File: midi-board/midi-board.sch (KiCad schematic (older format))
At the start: 39 parts, among them J1 MIDI OUT, J2 MIDI IN, J3 Qwiic, J4 A0, J5 A1, J6 Qwiic, J7 UART, U1 74LVC1G06, U2 MCP1X0-315, U3 TLP185(SE, U4 SC16IS740, X1 SG-5032CAN

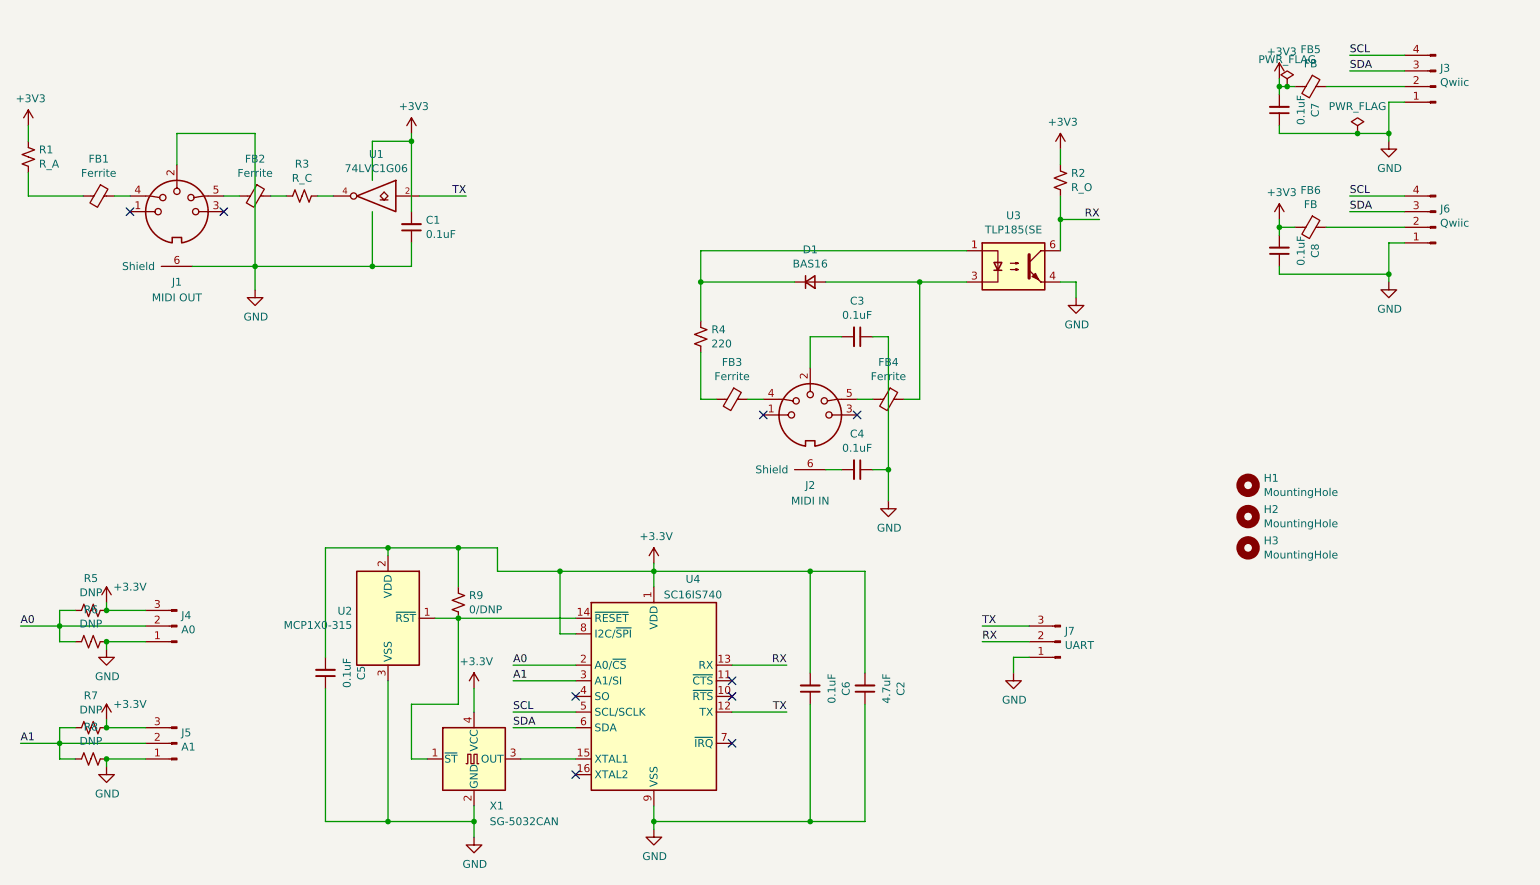
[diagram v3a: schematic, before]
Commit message: MIDI board Rev 1 changes
* Standardize mounting hole spacing
* Change 74LVC1G06 to 74LVC1G07 in schematic
* Expose ~IRQ headers
* Increase Qwiic header space
* Improve TLP185(SE footprint; remove unused pads, label orientation
* Bring I2C out on a header.
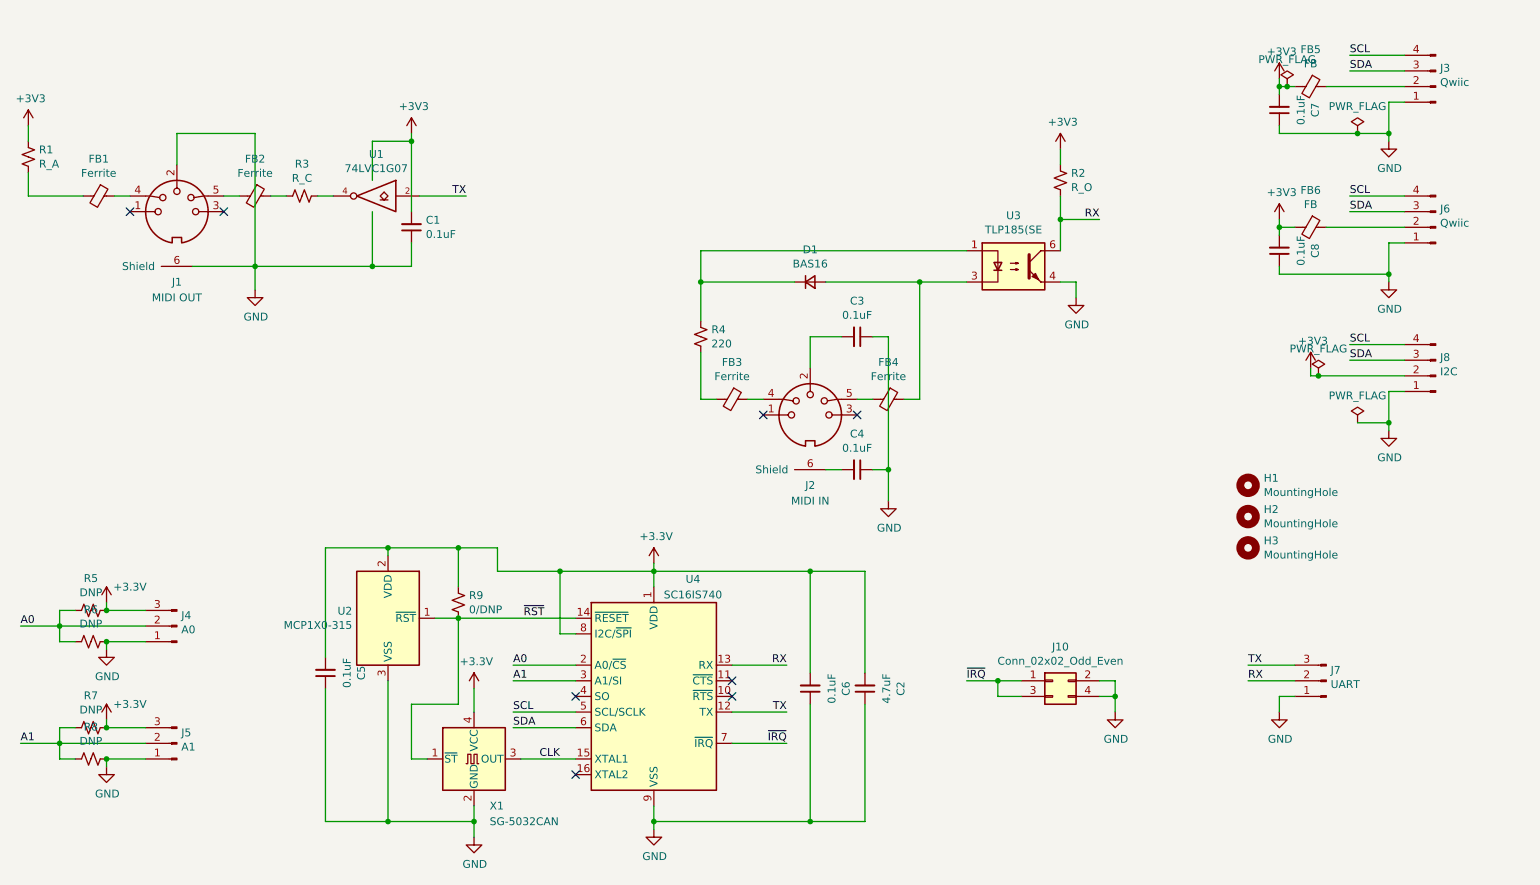
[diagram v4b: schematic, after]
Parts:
- added J10: Conn_02x02_Odd_Even, Pin_Headers:Pin_Header_Straight_2x02_Pitch2.54mm, symbol Connector_Generic:Conn_02x02_Odd_Even
- added J8: I2C, Pin_Headers:Pin_Header_Straight_1x04_Pitch2.54mm, symbol Connector:Conn_01x04_Male
- H1, H2, H3: footprint Mounting_Holes:MountingHole_3.2mm_M3 -> Mounting_Holes:MountingHole_3.2mm_M3_Pad_Via
- U1: value 74LVC1G06 -> 74LVC1G07
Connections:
- net +3V3: now also J8.2 (Pin_2)
- net GND: now also J10.2 (Pin_2), J10.4 (Pin_4), J8.1 (Pin_1)
- net SCL: now also J8.4 (Pin_4)
- net SDA: now also J8.3 (Pin_3)
- net ~RST: now reaches R9.1, U2.1 (~RST), U4.14 (~RESET), X1.1 (~ST)
- net CLK: now reaches U4.15 (XTAL1), X1.3 (OUT)
- net ~IRQ: now reaches U4.7 (~IRQ)
- net ~IRQ: now also J10.1 (Pin_1), J10.3 (Pin_3)
- no-connect marks 9 -> 8
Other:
- moved on the sheet: J7
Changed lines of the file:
@@
 P 3400 1950
 F 0 "U1" H 3375 2217 50  0000 C CNN
-F 1 "74LVC1G06" H 3375 2126 50  0000 C CNN
+F 1 "74LVC1G07" H 3375 2126 50  0000 C CNN
 F 2 "TO_SOT_Packages_SMD:SOT-353_SC-70-5_Handsoldering" H 3400 1950 50  0001 C CNN
 F 3 "http://www.ti.com/lit/sg/scyt129e/scyt129e.pdf" H 3400 1950 50  0001 C CNN
@@
 F 0 "H1" H 9100 3846 50  0000 L CNN
 F 1 "MountingHole" H 9100 3755 50  0000 L CNN
-F 2 "Mounting_Holes:MountingHole_3.2mm_M3" H 9000 3800 50  0001 C CNN
+F 2 "Mounting_Holes:MountingHole_3.2mm_M3_Pad_Via" H 9000 3800 50  0001 C CNN
 F 3 "~" H 9000 3800 50  0001 C CNN
 	1    9000 3800
@@
 F 0 "H2" H 9100 4046 50  0000 L CNN
 F 1 "MountingHole" H 9100 3955 50  0000 L CNN
-F 2 "Mounting_Holes:MountingHole_3.2mm_M3" H 9000 4000 50  0001 C CNN
+F 2 "Mounting_Holes:MountingHole_3.2mm_M3_Pad_Via" H 9000 4000 50  0001 C CNN
 F 3 "~" H 9000 4000 50  0001 C CNN
 	1    9000 4000
@@
 F 0 "H3" H 9100 4246 50  0000 L CNN
 F 1 "MountingHole" H 9100 4155 50  0000 L CNN
-F 2 "Mounting_Holes:MountingHole_3.2mm_M3" H 9000 4200 50  0001 C CNN
+F 2 "Mounting_Holes:MountingHole_3.2mm_M3_Pad_Via" H 9000 4200 50  0001 C CNN
 F 3 "~" H 9000 4200 50  0001 C CNN
 	1    9000 4200
@@
 NoConn ~ 5700 5150
 NoConn ~ 5700 5050
-NoConn ~ 5700 5450
 NoConn ~ 4700 5650
 Wire Wire Line
@@
 L Connector:Conn_01x03_Male J7
 U 1 1 5FFC58E3
-P 7800 4800
-F 0 "J7" H 7772 4732 50  0000 R CNN
-F 1 "UART" H 7772 4823 50  0000 R CNN
-F 2 "Pin_Headers:Pin_Header_Straight_1x03_Pitch2.54mm" H 7800 4800 50  0001 C CNN
-F 3 "~" H 7800 4800 50  0001 C CNN
-	1    7800 4800
-	-1   0    0    1
-$EndComp
-Wire Wire Line
-	7600 4900 7500 4900
-Wire Wire Line
-	7500 4900 7500 5000
+P 9500 5050
+F 0 "J7" H 9472 4982 50  0000 R CNN
+F 1 "UART" H 9472 5073 50  0000 R CNN
+F 2 "Pin_Headers:Pin_Header_Straight_1x03_Pitch2.54mm" H 9500 5050 50  0001 C CNN
+F 3 "~" H 9500 5050 50  0001 C CNN
+	1    9500 5050
+	-1   0    0    1
+$EndComp
+Wire Wire Line
+	9300 5150 9200 5150
+Wire Wire Line
+	9200 5150 9200 5250
 $Comp
 L power:GND #PWR0119
 U 1 1 5FFCB599
-P 7500 5000
-F 0 "#PWR0119" H 7500 4750 50  0001 C CNN
-F 1 "GND" H 7505 4827 50  0000 C CNN
-F 2 "" H 7500 5000 50  0001 C CNN
-F 3 "" H 7500 5000 50  0001 C CNN
-	1    7500 5000
-	1    0    0    -1
-$EndComp
-Wire Wire Line
-	7600 4800 7300 4800
-Wire Wire Line
-	7600 4700 7300 4700
-Text Label 7300 4700 0    50   ~ 0
+P 9200 5250
+F 0 "#PWR0119" H 9200 5000 50  0001 C CNN
+F 1 "GND" H 9205 5077 50  0000 C CNN
+F 2 "" H 9200 5250 50  0001 C CNN
+F 3 "" H 9200 5250 50  0001 C CNN
+	1    9200 5250
+	1    0    0    -1
+$EndComp
+Wire Wire Line
+	9300 5050 9000 5050
+Wire Wire Line
+	9300 4950 9000 4950
+Text Label 9000 4950 0    50   ~ 0
 TX
-Text Label 7300 4800 0    50   ~ 0
+Text Label 9000 5050 0    50   ~ 0
 RX
 Wire Wire Line
@@
 Wire Wire Line
 	9700 1550 9900 1550
+$Comp
+L Connector_Generic:Conn_02x02_Odd_Even J10
+U 1 1 6006C764
+P 7750 5050
+F 0 "J10" H 7800 5267 50  0000 C CNN
+F 1 "Conn_02x02_Odd_Even" H 7800 5176 50  0000 C CNN
+F 2 "Pin_Headers:Pin_Header_Straight_2x02_Pitch2.54mm" H 7750 5050 50  0001 C CNN
+F 3 "~" H 7750 5050 50  0001 C CNN
+	1    7750 5050
+	1    0    0    -1
+$EndComp
+$Comp
+L power:GND #PWR0120
+U 1 1 6006CF1A
+P 8150 5250
+F 0 "#PWR0120" H 8150 5000 50  0001 C CNN
+F 1 "GND" H 8155 5077 50  0000 C CNN
+F 2 "" H 8150 5250 50  0001 C CNN
+F 3 "" H 8150 5250 50  0001 C CNN
+	1    8150 5250
+	1    0    0    -1
+$EndComp
+Wire Wire Line
+	8050 5050 8150 5050
+Wire Wire Line
+	8150 5050 8150 5150
+Wire Wire Line
+	8050 5150 8150 5150
+Connection ~ 8150 5150
+Wire Wire Line
+	8150 5150 8150 5250
+Wire Wire Line
+	7200 5050 7400 5050
+Wire Wire Line
+	7400 5050 7400 5150
+Wire Wire Line
+	7400 5150 7550 5150
+Connection ~ 7400 5050
+Wire Wire Line
+	7400 5050 7550 5050
+Text Label 7200 5050 0    50   ~ 0
+~IRQ
+Wire Wire Line
+	5700 5450 6050 5450
+Text Label 6050 5450 2    50   ~ 0
+~IRQ
+$Comp
+L Connector:Conn_01x04_Male J8
+U 1 1 600A655B
+P 10200 3100
+F 0 "J8" H 10172 2982 50  0000 R CNN
+F 1 "I2C" H 10172 3073 50  0000 R CNN
+F 2 "Pin_Headers:Pin_Header_Straight_1x04_Pitch2.54mm" H 10200 3100 50  0001 C CNN
+F 3 "~" H 10200 3100 50  0001 C CNN
+	1    10200 3100
+	-1   0    0    1
+$EndComp
+$Comp
+L power:+3V3 #PWR0123
+U 1 1 600A6561
+P 9400 3050
+F 0 "#PWR0123" H 9400 2900 50  0001 C CNN
+F 1 "+3V3" H 9415 3223 50  0000 C CNN
+F 2 "" H 9400 3050 50  0001 C CNN
+F 3 "" H 9400 3050 50  0001 C CNN
+	1    9400 3050
+	1    0    0    -1
+$EndComp
+$Comp
+L power:GND #PWR0124
+U 1 1 600A6567
+P 9900 3450
+F 0 "#PWR0124" H 9900 3200 50  0001 C CNN
+F 1 "GND" H 9905 3277 50  0000 C CNN
+F 2 "" H 9900 3450 50  0001 C CNN
+F 3 "" H 9900 3450 50  0001 C CNN
+	1    9900 3450
+	1    0    0    -1
+$EndComp
+Wire Wire Line
+	9400 3050 9400 3100
+Wire Wire Line
+	9400 3100 9450 3100
+Wire Wire Line
+	10000 3200 9900 3200
+Wire Wire Line
+	9900 3200 9900 3400
+Wire Wire Line
+	10000 3000 9650 3000
+Wire Wire Line
+	10000 2900 9650 2900
+Text Label 9650 2900 0    50   ~ 0
+SCL
+Text Label 9650 3000 0    50   ~ 0
+SDA
+Connection ~ 9900 3400
+Wire Wire Line
+	9900 3400 9900 3450
+$Comp
+L power:PWR_FLAG #FLG0103
+U 1 1 600A6588
+P 9450 3100
+F 0 "#FLG0103" H 9450 3175 50  0001 C CNN
+F 1 "PWR_FLAG" H 9450 3273 50  0000 C CNN
+F 2 "" H 9450 3100 50  0001 C CNN
+F 3 "~" H 9450 3100 50  0001 C CNN
+	1    9450 3100
+	1    0    0    -1
+$EndComp
+$Comp
+L power:PWR_FLAG #FLG0104
+U 1 1 600A6590
+P 9700 3400
+F 0 "#FLG0104" H 9700 3475 50  0001 C CNN
+F 1 "PWR_FLAG" H 9700 3573 50  0000 C CNN
+F 2 "" H 9700 3400 50  0001 C CNN
+F 3 "~" H 9700 3400 50  0001 C CNN
+	1    9700 3400
+	1    0    0    -1
+$EndComp
+Wire Wire Line
+	9700 3400 9900 3400
+Wire Wire Line
+	10000 3100 9450 3100
+Connection ~ 9450 3100
+Text Label 4500 4650 2    50   ~ 0
+~RST
+Text Label 4600 5550 2    50   ~ 0
+CLK
 $EndSCHEMATC
